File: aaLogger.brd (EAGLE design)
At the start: 88.9 x 48.3 mm, 55 parts, among them Q1 IRLML6244TR, U1 MCP1640C, U2 ATmega328P-AU

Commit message: Near final.
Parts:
- added C10, C9: 27pF, _jc:M0805
- added C11, C13: 100nF, _jc:M0805
- added JMP1: solder jumper, _jc:M0805
- added JP3: GNDSEL, SparkFun:1X03_LOCK
- added JP4: RTC BACKUP, SparkFun:1X03_LOCK
- added LOGO1, LOGO2: OSHW_LOGO_8MILX0150-NT, ohw-logo:OSHW_8X150_NOTEXT
- added PR13: (no value), _jc:PROTO-3
- B1: value (none) -> CR2016
- C1: value 100nF -> 10uF; device _jc:C0805 -> _jc:M0805
- C12, C4, C5, C6, C7, C8: device _jc:C0805 -> _jc:M0805
- J1: value (none) -> ICSP
- L1: device _jc:R1210 -> _jc:NRS5020
- PR1, PR10, PR11, PR12, PR2, PR3, PR4, PR5, PR6, PR7, PR8, PR9: value PROTO-5 -> PROTO-10; device _jc:PROTO-5 -> _jc:PROTO-10
- R10: value 249K -> 2.2K
- R11: value solder jumper -> 10K
- R12: value 100 -> 220
- R3: value 47.5K -> 249K
- R4: value 10K -> 47.5K
- R5: value 2.2K -> 10K
- R6: device _jc:R0805 -> _jc:M0805
- S1: value (none) -> RESET
- S2: value (none) -> START/INIT
- S3: value (none) -> DL/SET
- TB1: value 3 - 4.5VDC -> +BAT-
- U3: value (none) -> DS3232
- U4, U5: value (none) -> M24M02
- Y1: value (none) -> 8MHz; device _jc:ZTT-RESONATOR -> _jc:RESONATOR
- moved R4 48.8 mm to (12.4, 13.7)
- moved C7 26.7 mm to (52.8, 16.9), turned to 0 degrees
- moved C8 22.6 mm to (52.8, 21.2), turned to 0 degrees
- moved R3 21.7 mm to (23.6, 30.4), turned to 180 degrees
- moved C6 21.5 mm to (34.7, 22.0), turned to 180 degrees
- moved R8 19.2 mm to (56.4, 8.64)
- moved R9 17.8 mm to (36.3, 27.9)
- moved C5 16.9 mm to (52.6, 35.9)
- moved R5 15.9 mm to (58.4, 22.9), turned to 0 degrees
- moved PR1 14.5 mm to (82.5, 39.4), turned to 0 degrees
- moved C12 13.1 mm to (47.9, 44.3)
- moved C4 12.2 mm to (58.4, 25.7)
- moved C1 11.3 mm to (23.9, 16.5), turned to 0 degrees
- moved C3 10.7 mm to (30.4, 22.9)
- moved U$2 10.2 mm to (96.5, 25.4)
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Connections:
- removed net /WC: U2.32, U4.7, U5.7
- removed net PGND: Q1.3, U$2.PAD01, U$2.PAD02, U$2.PAD03, U$2.PAD04, U$2.PAD05, U$2.PAD06, U$2.PAD07, U$2.PAD08, U$2.PAD09, U$2.PAD10, U$2.PAD11, U$2.PAD12, U3.1, U3.10, U3.11, U3.12, U3.13, U3.14, U3.15, U3.19, U3.2, U3.7, U3.8, U3.9, U4.3, U4.4, U5.4
- new net N$10: PR3.10, PR3.6, PR3.7, PR3.8, PR3.9
- new net N$14: PR4.10, PR4.6, PR4.7, PR4.8, PR4.9
- new net N$15: PR6.10, PR6.6, PR6.7, PR6.8, PR6.9
- new net N$28: PR7.10, PR7.6, PR7.7, PR7.8, PR7.9
- new net N$30: PR8.10, PR8.6, PR8.7, PR8.8, PR8.9
- new net N$31: PR9.10, PR9.6, PR9.7, PR9.8, PR9.9
- new net N$32: PR10.10, PR10.6, PR10.7, PR10.8, PR10.9
- new net N$33: PR11.10, PR11.6, PR11.7, PR11.8, PR11.9
- new net N$34: PR12.10, PR12.6, PR12.7, PR12.8, PR12.9
- new net N$35: JP4.2, U3.16
- new net N$36: JP3.1, Q1.3
- new net N$4: PR1.10, PR1.6, PR1.7, PR1.8, PR1.9
- new net N$5: PR5.10, PR5.6, PR5.7, PR5.8, PR5.9
- new net N$9: PR2.10, PR2.6, PR2.7, PR2.8, PR2.9
- new net SGND: JP3.2, U$2.1, U$2.10, U$2.11, U$2.12, U$2.2, U$2.3, U$2.4, U$2.5, U$2.6, U$2.7, U$2.8, U$2.9
- new net SPWR: R12.2, U2.13
- net /RESET: now also C5.1; no longer C12.1
- net 32KHZ: now also R11.1
- net ADC6: now also C4.2, R5.2; no longer R4.2
- net ADC7: now also C4.1, R4.2, R5.1; no longer R3.2, R4.1
- net BAT: now also C1.1, JP4.1, L1.P$1, R4.1; no longer C2.1, L1.1, R3.1
- net GND: now also C10.2, C11.2, C12.2, C13.2, C9.2, JMP1.2, JP3.3, PR13.1, PR13.2, PR13.3, R3.2, U3.1, U3.10, U3.11, U3.12, U3.13, U3.14, U3.15, U3.19, U3.2, U3.7, U3.8, U3.9, U4.3, U4.4, U4.7, U5.4, U5.7; no longer C4.2, C5.2, R10.2, R11.2
- net LED1: now also R7.2; no longer R5.2
- net LED2: now also R8.2; no longer R7.2
- net MISO: now also JP1.11; no longer JP1.10
- net MOSI: now also JP1.12; no longer JP1.11
- net N$1: now also JP4.3; no longer U3.16
- net N$11: now also C10.1
- net N$12: now also JMP1.1, R3.1; no longer R10.1, R11.1
- net N$13: now also C8.1; no longer C5.1
- net N$2: now also R7.1; no longer R5.1
- net N$3: now also R8.1; no longer R7.1
- net N$7: now also L1.P$2; no longer L1.2
- net N$8: now also C9.1
- net PPWR: now also C11.1, C12.1, C13.1, U2.32, U3.4, U4.8, U5.3, U5.8; no longer R12.2, U2.13
- net RST: now also C5.2; no longer C12.2
- net SCK: now also JP1.10; no longer JP1.12
- net SCL: now also R10.1; no longer R9.1
- net SDA: now also R9.1; no longer R8.1
- net SW2: now also U2.10; no longer U2.9
- net SW3: now also U2.9; no longer U2.10
- net VCC: now also C2.1, R10.2, R11.2, U$1.1, U$1.10, U$1.11, U$1.12, U$1.2, U$1.3, U$1.4, U$1.5, U$1.6, U$1.7, U$1.8, U$1.9; no longer C1.1, C4.1, C8.1, R8.2, U$1.PAD01, U$1.PAD02, U$1.PAD03, U$1.PAD04, U$1.PAD05, U$1.PAD06, U$1.PAD07, U$1.PAD08, U$1.PAD09, U$1.PAD10, U$1.PAD11, U$1.PAD12, U3.4, U4.8, U5.3, U5.8
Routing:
- net PGND: track 135.6 -> 0.00 mm, vias 3 -> 0
- net VCC: track 177.4 -> 132.2 mm
- net SGND: track 0.00 -> 42.3 mm
- net SPWR: track 0.00 -> 41.1 mm
- net /WC: track 40.6 -> 0.00 mm, vias 3 -> 0
- net BAT: track 26.4 -> 59.5 mm
- net N$35: track 0.00 -> 24.9 mm
- net PPWR: track 33.2 -> 56.5 mm
- net N$1: track 27.1 -> 4.21 mm
- net GND: track 0.00 -> 19.7 mm, vias 4 -> 12
- net 32KHZ: track 39.7 -> 51.3 mm, vias 1 -> 2
- net N$9: track 0.00 -> 10.2 mm
- net N$5: track 0.00 -> 10.2 mm
- net N$4: track 0.00 -> 10.2 mm
- net N$34: track 0.00 -> 10.2 mm
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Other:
- board size 88.9 x 48.3 mm -> 99.1 x 49.5 mm
- board text added: "0"
- board text added: "1"
- board text added: "32K"
- board text added: "A0"
- board text added: "A1"
- board text added: "A2"
- board text added: "A3"
- board text added: "A6"
- board text added: "AA"
- board text added: "BATT"
- board text added: "BLK"
- board text added: "CC BY-SA jc 0213 v1"
- board text added: "COIN"
- board text added: "DWNLD/SET"
- board text added: "Double-A Datalogger"
- board text added: "FOR 5V"
- board text added: "FTDI"
- board text added: "GND"
- board text added: "GRN"
- board text added: "ICSP"
- board text added: "MISO/12"
- board text added: "MOSI/11"
- board text added: "RESET"
- board text added: "RTC"
- board text added: "SCK/13"
- board text added: "SCL"
- board text added: "SDA"
- board text added: "SGND"
- board text added: "SOLDER"
- board text added: "SS/10"
- board text added: "START/INIT"
- board text added: "Vcc"
- board text added: "open source"

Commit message: v1 as sent to iTead.
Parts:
- JP1: value M12PTH -> PROTO-12NR; device SparkFun:1X12 -> _jc:PROTO-12-NR
- R7, R8: value 2.2K -> 1K
- U$1, U$2: value PROTO-12 -> PROTO-12PROTO
- moved JP1 14.0 mm to (64.8, 25.4)
- moved LOGO2 1.27 mm to (10.9, 16.5)
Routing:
- net GND: vias 12 -> 13
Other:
- board text added: "100009672"
- board text added: "CC BY-SA jc 0313 v1"
- board text added: "Double-A DataLogger"
- board text removed: "CC BY-SA jc 0213 v1"
- board text removed: "Double-A Datalogger"

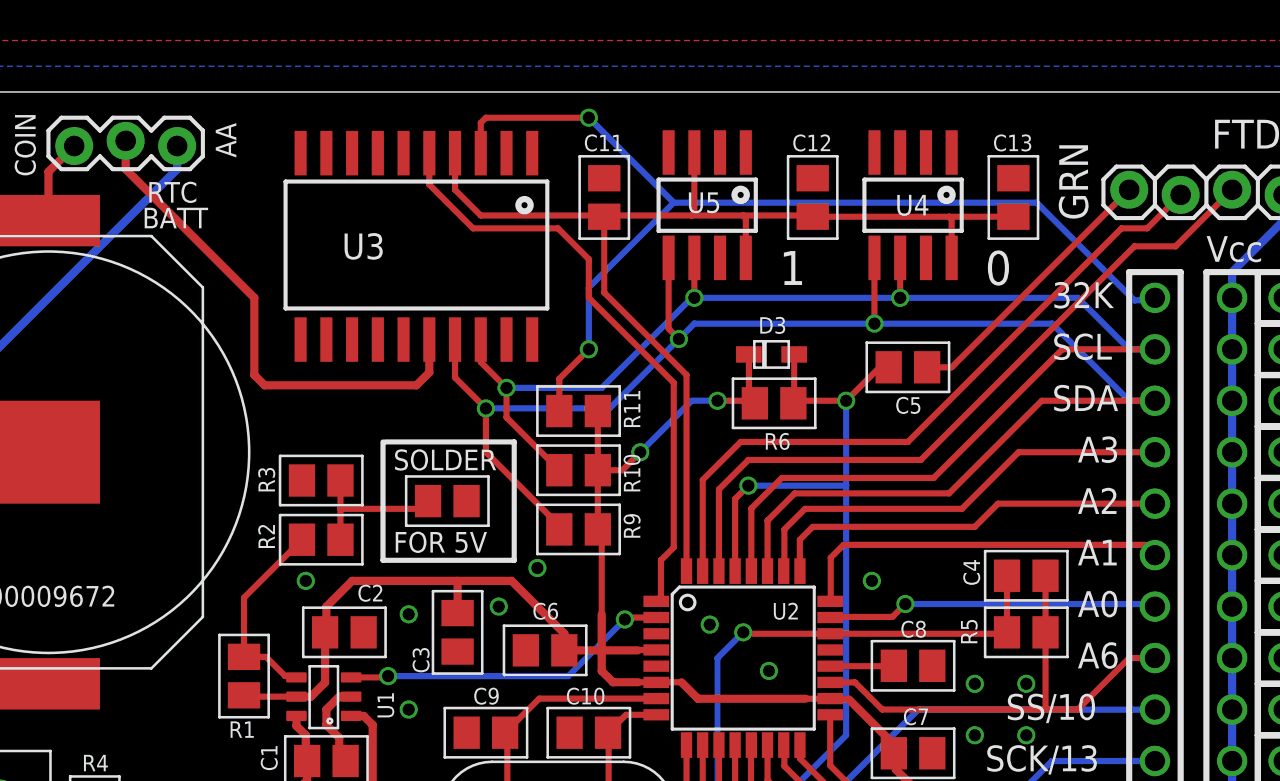
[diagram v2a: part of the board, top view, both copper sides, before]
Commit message: Remove R11, not needed. Reroute 32K, move RTC slightly.
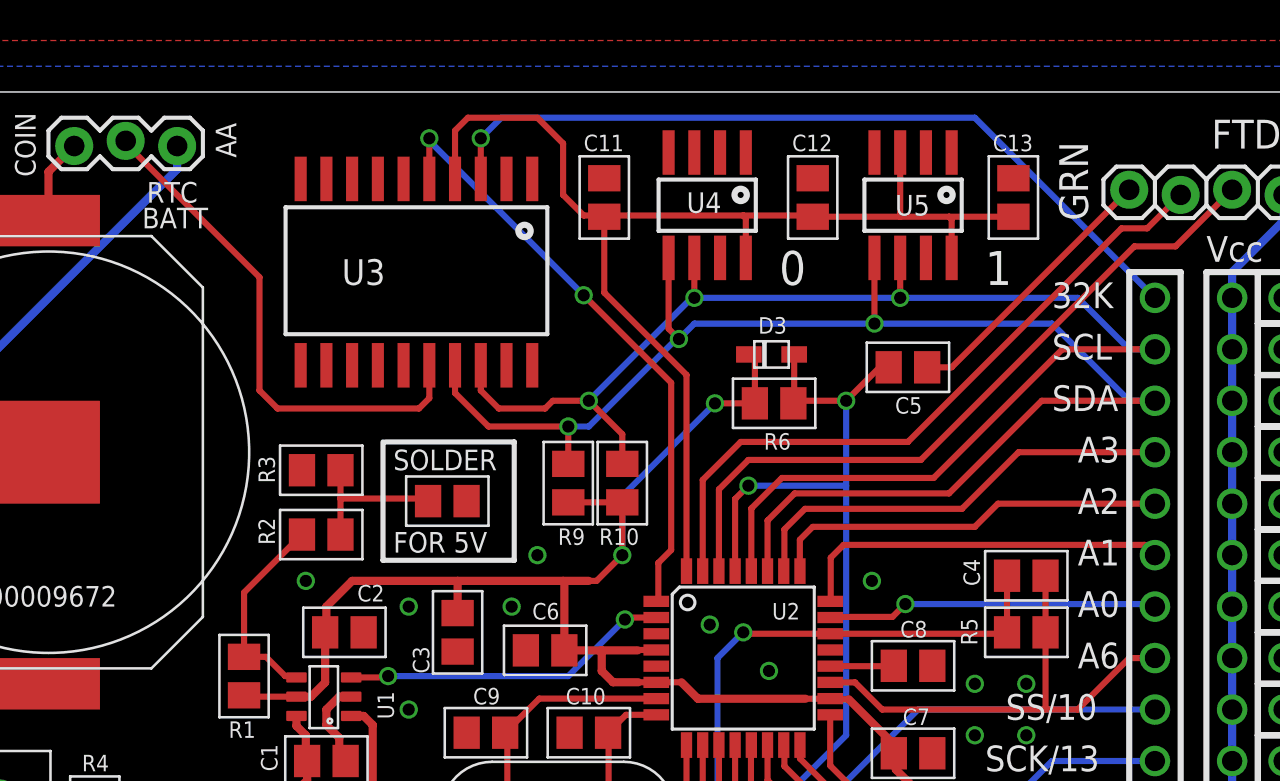
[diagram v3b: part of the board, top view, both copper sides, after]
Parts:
- removed R11: 10K, _jc:M0805
- moved U4 10.2 mm to (42.7, 43.9)
- moved U5 10.2 mm to (52.8, 43.9)
- moved R9 2.34 mm to (35.8, 30.2), turned to 270 degrees
- moved R10 2.25 mm to (38.5, 30.2), turned to 270 degrees
- moved LOGO2 1.27 mm to (10.9, 17.8)
- moved U3 1.27 mm to (28.3, 40.6)
- moved R3 0.51 mm to (23.6, 30.9)
- moved R2 0.25 mm to (23.6, 27.7)
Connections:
- net 32KHZ: no longer R11.1
- net VCC: no longer R11.2
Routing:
- net 32KHZ: track 51.3 -> 39.4 mm, vias 2 -> 1
- net SDA: track 79.7 -> 73.7 mm
- net PPWR: track 56.5 -> 60.4 mm
- net SCL: track 73.8 -> 72.4 mm
- net VCC: track 132.5 -> 133.4 mm
- net N$35: track 24.9 -> 25.6 mm
- net INT: track 29.9 -> 30.1 mm, vias 0 -> 2
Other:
- board text added: "CC BY-SA jc 0313 v2"
- board text added: "Double-A Data Logger"
- board text removed: "CC BY-SA jc 0313 v1"
- board text removed: "Double-A DataLogger"

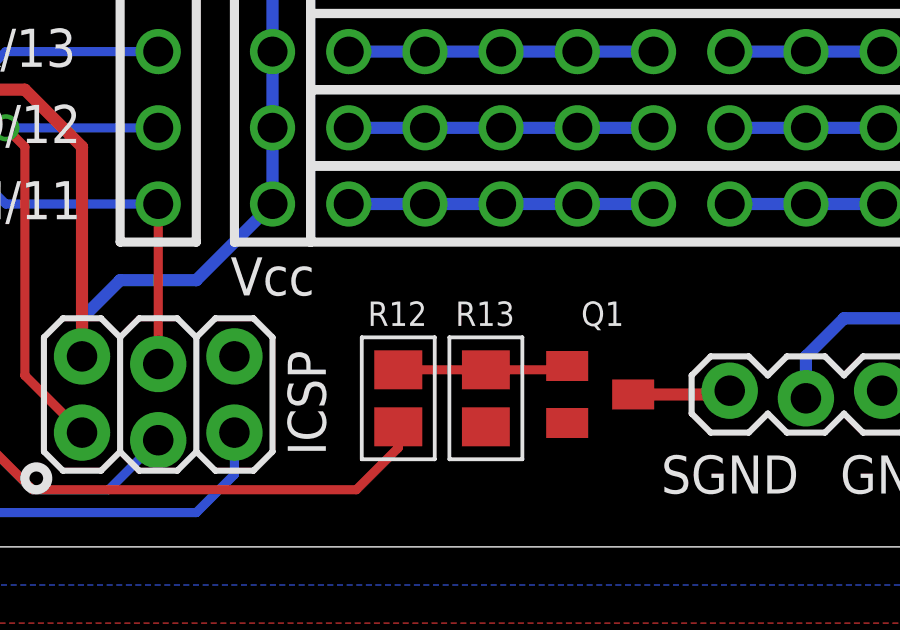
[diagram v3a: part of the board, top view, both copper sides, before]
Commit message: Rename resistors. Tweak schematic layout, titles. Put github URL on bottom of board.
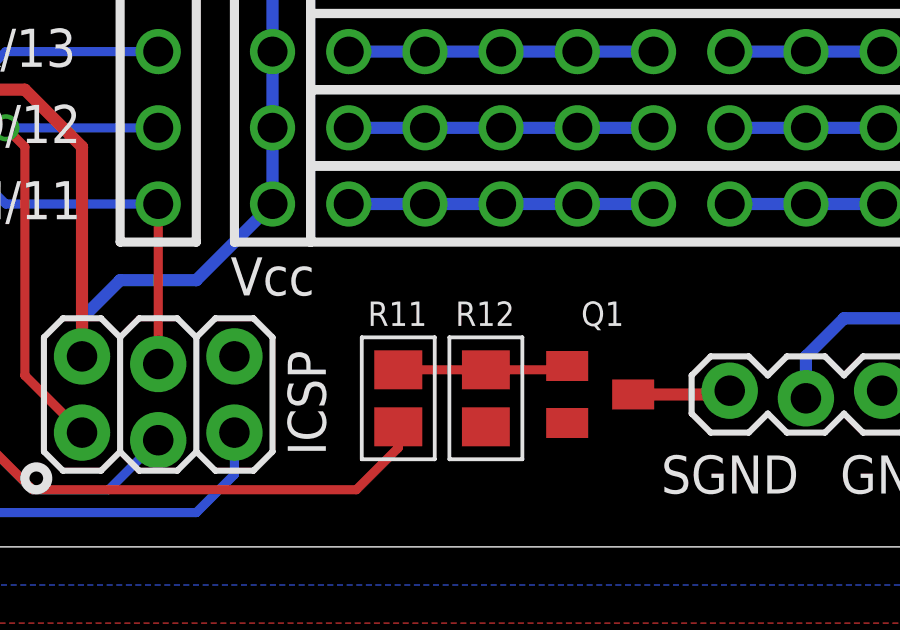
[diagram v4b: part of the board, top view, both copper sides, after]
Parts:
- removed R13: 10K, _jc:M0805
- added R11: 220, _jc:M0805
- R12: value 220 -> 10K
- moved R12 2.92 mm to (75.7, 4.95)
- moved LOGO2 2.84 mm to (12.2, 15.2)
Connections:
- net GND: now also R12.2; no longer R13.2
- net N$24: now also R11.1; no longer R13.1
- net SPWR: now also R11.2; no longer R12.2
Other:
- board text added: "http://github.com/JChristensen"
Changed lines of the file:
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@@
 <text x="56.388" y="40.005" size="1.6764" layer="21" ratio="12">1</text>
 <text x="46.228" y="40.005" size="1.6764" layer="21" ratio="12">0</text>
-<text x="19.05" y="13.97" size="1.6764" layer="22" ratio="12" rot="MR90">Double-A Data Logger</text>
-<text x="15.621" y="13.843" size="1.6764" layer="22" ratio="12" rot="MR90">CC BY-SA jc 0313 v2</text>
-<text x="12.065" y="22.86" size="1.4224" layer="22" ratio="12" rot="MR90">open source</text>
+<text x="20.32" y="11.43" size="1.6764" layer="22" ratio="12" rot="MR90">Double-A Data Logger</text>
+<text x="16.891" y="11.303" size="1.6764" layer="22" ratio="12" rot="MR90">CC BY-SA jc 0313 v2</text>
+<text x="13.335" y="20.32" size="1.4224" layer="22" ratio="12" rot="MR90">open source</text>
 <rectangle x1="21.844" y1="13.843" x2="25.654" y2="15.494" layer="41"/>
 <rectangle x1="22.86" y1="17.272" x2="24.638" y2="21.209" layer="41"/>
 <text x="6.35" y="24.13" size="1.016" layer="21" ratio="10">100009672</text>
-<text x="8.89" y="22.86" size="1.016" layer="22" ratio="10" rot="MR90">100009672</text>
+<text x="90.17" y="46.99" size="1.016" layer="22" ratio="10" rot="MR0">100009672</text>
+<text x="10.16" y="11.43" size="1.27" layer="22" ratio="10" rot="MR90">http://github.com/JChristensen</text>
 </plain>
 <attributes>
@@
 <attribute name="VALUE" x="76.327" y="6.985" size="1.016" layer="27" ratio="10" rot="R270"/>
 </element>
-<element name="R12" library="_jc" package="M0805" value="220" x="72.771" y="4.953" smashed="yes" rot="R270">
+<element name="R11" library="_jc" package="M0805" value="220" x="72.771" y="4.953" smashed="yes" rot="R270">
 <attribute name="NAME" x="71.755" y="7.366" size="0.8128" layer="25" ratio="10"/>
 <attribute name="VALUE" x="70.485" y="5.969" size="0.8128" layer="27" ratio="10" rot="R270"/>
 </element>
-<element name="R13" library="_jc" package="M0805" value="10K" x="75.692" y="4.953" smashed="yes" rot="R270">
+<element name="R12" library="_jc" package="M0805" value="10K" x="75.692" y="4.953" smashed="yes" rot="R270">
 <attribute name="NAME" x="74.676" y="7.366" size="0.8128" layer="25" ratio="10"/>
 <attribute name="VALUE" x="73.406" y="5.969" size="0.8128" layer="27" ratio="10" rot="R270"/>
@@
 </element>
 <element name="LOGO1" library="ohw-logo" package="OSHW_8X150_NOTEXT" value="OSHW_LOGO_8MILX0150-NT" x="8.001" y="2.032"/>
-<element name="LOGO2" library="ohw-logo" package="OSHW_8X150_NOTEXT" value="OSHW_LOGO_8MILX0150-NT" x="10.922" y="17.78" rot="MR90"/>
+<element name="LOGO2" library="ohw-logo" package="OSHW_8X150_NOTEXT" value="OSHW_LOGO_8MILX0150-NT" x="12.192" y="15.24" rot="MR90"/>
 </elements>
 <signals>
@@
 <contactref element="S1" pad="3"/>
 <contactref element="Q1" pad="2"/>
-<contactref element="R13" pad="2"/>
+<contactref element="R12" pad="2"/>
 <polygon width="0.254" layer="1" isolate="0.3048">
 <vertex x="-2.54" y="52.07"/>
@@
 <signal name="N$24">
 <contactref element="Q1" pad="1"/>
+<contactref element="R11" pad="1"/>
 <contactref element="R12" pad="1"/>
-<contactref element="R13" pad="1"/>
-<contactref element="R13" pad="1"/>
+<contactref element="R12" pad="1"/>
 <wire x1="72.771" y1="5.903" x2="75.692" y2="5.903" width="0.3048" layer="1"/>
 <wire x1="75.692" y1="5.903" x2="78.275" y2="5.903" width="0.3048" layer="1"/>
@@
 </signal>
 <signal name="SPWR">
-<contactref element="R12" pad="2"/>
+<contactref element="R11" pad="2"/>
 <contactref element="U2" pad="13"/>
 <wire x1="44.85" y1="17.2974" x2="44.831" y2="17.2784" width="0.3048" layer="1"/>
